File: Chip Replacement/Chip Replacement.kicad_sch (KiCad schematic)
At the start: 2 parts, among them J2 Conn_01x14_Socket, U1 BGA153 UFS Modified

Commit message: V1.1
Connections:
- net REF_CLK: now also J2.5 (Pin_5); no longer J2.9 (Pin_9)
- net RST_N: now also J2.6 (Pin_6); no longer J2.8 (Pin_8)
- net RX0P: now also J2.8 (Pin_8); no longer J2.6 (Pin_6)
- net RX1N: now also J2.9 (Pin_9); no longer J2.5 (Pin_5)
- net RX1P: now also J2.10 (Pin_10); no longer J2.4 (Pin_4)
- net TX0N: now also J2.4 (Pin_4); no longer J2.10 (Pin_10)
- net TX0P: now also J2.3 (Pin_3); no longer J2.11 (Pin_11)
- net TX1N: now also J2.2 (Pin_2); no longer J2.12 (Pin_12)
- net TX1P: now also J2.1 (Pin_1); no longer J2.13 (Pin_13)
- net VCC: now also J2.11 (Pin_11); no longer J2.1 (Pin_1)
- net VCCQ: now also J2.13 (Pin_13); no longer J2.2 (Pin_2)
- net VCCQ2: now also J2.12 (Pin_12); no longer J2.3 (Pin_3)

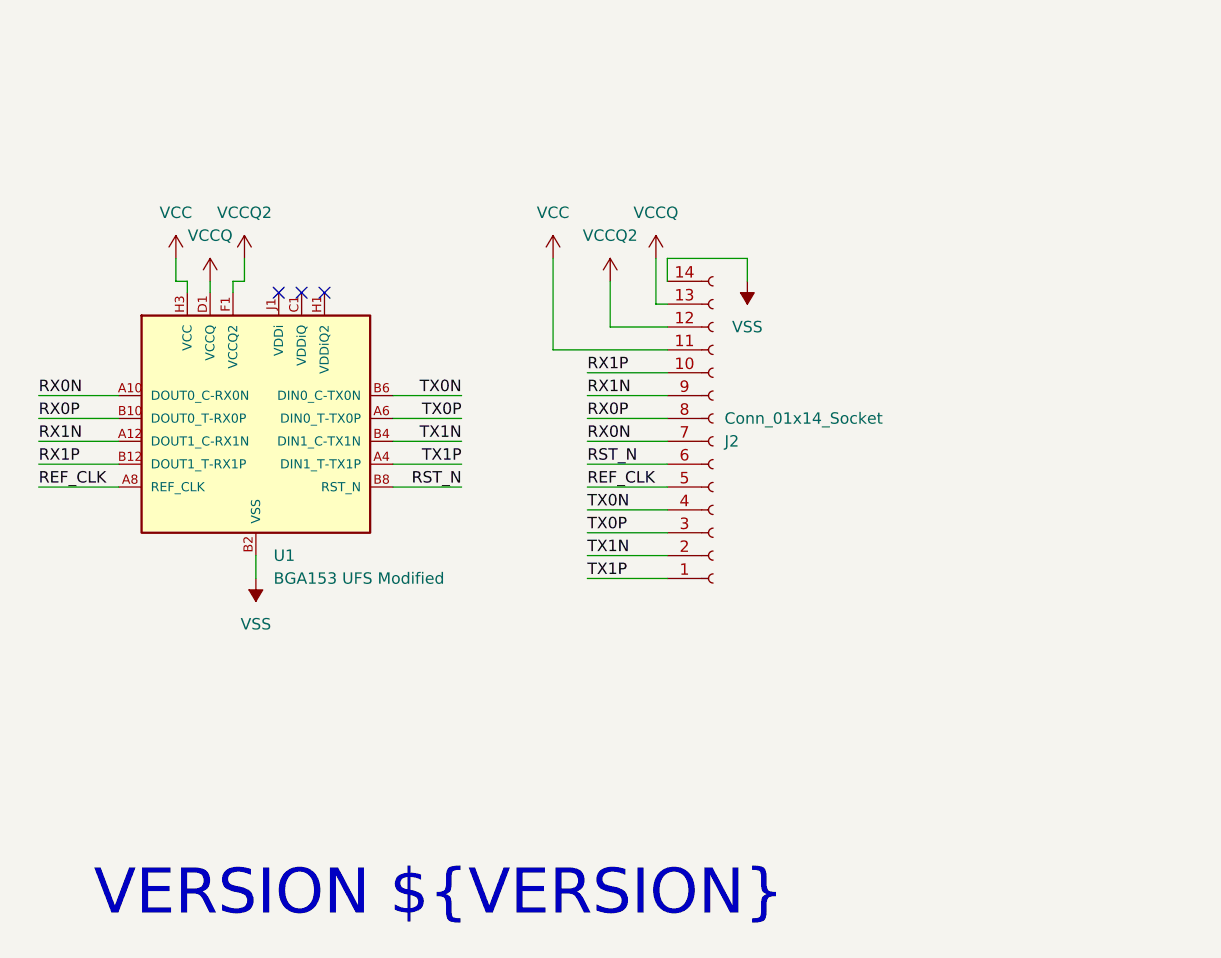
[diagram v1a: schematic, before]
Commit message: V1.2 for forward fpc cable
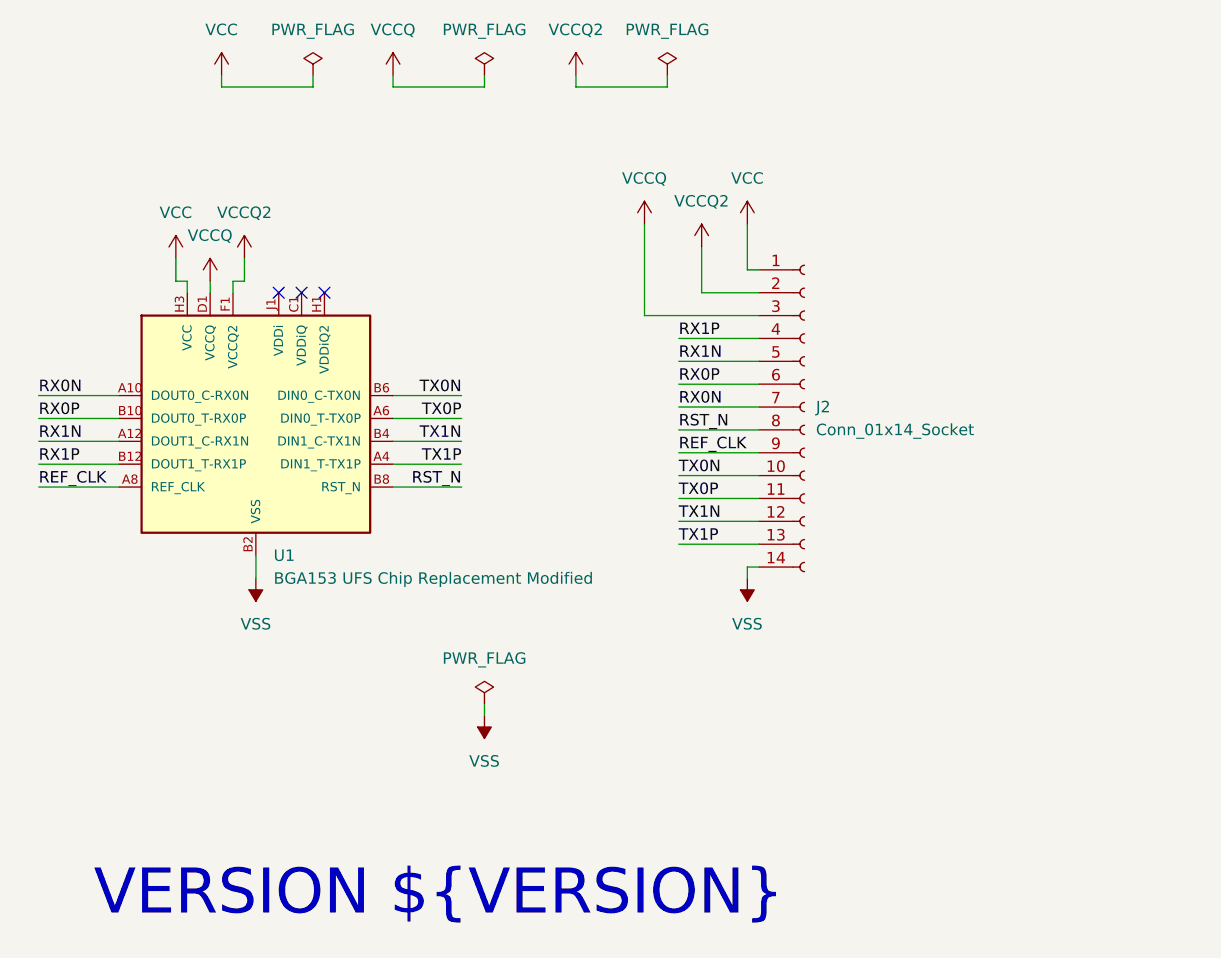
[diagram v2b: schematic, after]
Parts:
- U1: value BGA153 UFS Modified -> BGA153 UFS Chip Replacement Modified; symbol BGA153:BGA153 UFS Modified -> BGA153:BGA153 UFS Chip Replacement Modified
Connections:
- net REF_CLK: now also J2.9 (Pin_9); no longer J2.5 (Pin_5)
- net RST_N: now also J2.8 (Pin_8); no longer J2.6 (Pin_6)
- net RX0P: now also J2.6 (Pin_6); no longer J2.8 (Pin_8)
- net RX1N: now also J2.5 (Pin_5); no longer J2.9 (Pin_9)
- net RX1P: now also J2.4 (Pin_4); no longer J2.10 (Pin_10)
- net TX0N: now also J2.10 (Pin_10); no longer J2.4 (Pin_4)
- net TX0P: now also J2.11 (Pin_11); no longer J2.3 (Pin_3)
- net TX1N: now also J2.12 (Pin_12); no longer J2.2 (Pin_2)
- net TX1P: now also J2.13 (Pin_13); no longer J2.1 (Pin_1)
- net VCC: now also J2.1 (Pin_1); no longer J2.11 (Pin_11)
- net VCCQ: now also J2.3 (Pin_3); no longer J2.13 (Pin_13)
- net VCCQ2: now also J2.2 (Pin_2); no longer J2.12 (Pin_12)

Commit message: V1.3 GB042 Connector
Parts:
- removed J2: Conn_01x14_Socket, BGA153:FPC 14 Pin 0.5P, symbol Connector:Conn_01x14_Socket
- added J1: GB042-30S-H10, BGA153:GB042-30S-H10, symbol BGA153:GB042-30S-H10
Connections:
- net REF_CLK: now also J1.8 (Pin_8)
- net RST_N: now also J1.23 (Pin_23)
- net RX0N: now also J1.10 (Pin_10)
- net RX0P: now also J1.11 (Pin_11)
- net RX1N: now also J1.13 (Pin_13)
- net RX1P: now also J1.14 (Pin_14)
- net TX0N: now also J1.6 (Pin_6)
- net TX0P: now also J1.5 (Pin_5)
- net TX1N: now also J1.3 (Pin_3)
- net TX1P: now also J1.2 (Pin_2)
- net VCC: now also J1.17 (Pin_17)
- net VCCQ: now also J1.19 (Pin_19)
- net VCCQ2: now also J1.21 (Pin_21)
- net VSS: now also U1.B3 (VSS), J1.1 (Pin_1), J1.12 (Pin_12), J1.15 (Pin_15), J1.16 (Pin_16), J1.18 (Pin_18), J1.20 (Pin_20), J1.22 (Pin_22), J1.24 (Pin_24), J1.26 (Pin_26), J1.28 (Pin_28), J1.30 (Pin_30), J1.4 (Pin_4), J1.7 (Pin_7), J1.9 (Pin_9); no longer U1.B13 (VSS)
- net VDDiQ: now reaches U1.C1 (VDDiQ)
- net VDDiQ: now also J1.25 (Pin_25)
- net VDDiQ2: now reaches U1.H1 (VDDiQ2)
- net VDDiQ2: now also J1.27 (Pin_27)
- net VDDi: now reaches U1.J1 (VDDi)
- net VDDi: now also J1.29 (Pin_29)
- no-connect marks 3 -> 0
